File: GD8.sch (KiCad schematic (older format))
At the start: 19 parts, among them IC10 IXDD614PI, IC9 HCPL-316J, P8 CONN_01X03, P9 CONN_01X03

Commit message: uding HCPL-361J modified symbol
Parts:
- IC9: symbol HCPL-316J-RESCUE-gatedrive -> HCPL-316J
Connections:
- wire segments 41 -> 50
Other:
- moved on the sheet: IC10
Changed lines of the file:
@@
 EESchema Schematic File Version 2
-LIBS:gatedrive-rescue
 LIBS:power
 LIBS:device
@@
 LIBS:contrib
 LIBS:valves
-LIBS:GateDrive
+LIBS:74xgxx
+LIBS:ac-dc
+LIBS:actel
+LIBS:Altera
+LIBS:analog_devices
+LIBS:brooktre
+LIBS:cmos_ieee
+LIBS:dc-dc
+LIBS:diode
+LIBS:elec-unifil
+LIBS:ESD_Protection
+LIBS:ftdi
+LIBS:gennum
+LIBS:graphic
+LIBS:hc11
+LIBS:ir
+LIBS:Lattice
+LIBS:logo
+LIBS:maxim
+LIBS:microchip_dspic33dsc
+LIBS:microchip_pic10mcu
+LIBS:microchip_pic12mcu
+LIBS:microchip_pic16mcu
+LIBS:microchip_pic18mcu
+LIBS:microchip_pic32mcu
+LIBS:motor_drivers
+LIBS:msp430
+LIBS:nordicsemi
+LIBS:nxp_armmcu
+LIBS:onsemi
+LIBS:Oscillators
+LIBS:powerint
+LIBS:Power_Management
+LIBS:pspice
+LIBS:references
+LIBS:relays
+LIBS:rfcom
+LIBS:sensors
+LIBS:silabs
+LIBS:stm8
+LIBS:stm32
+LIBS:supertex
+LIBS:switches
+LIBS:transf
+LIBS:ttl_ieee
+LIBS:video
+LIBS:Worldsemi
+LIBS:Xicor
+LIBS:Zilog
 LIBS:gatedrive-cache
 EELAYER 25 0
@@
 L IXDD614PI-RESCUE-gatedrive IC10
 U 1 1 56EFD9AC
-P 7900 5100
-F 0 "IC10" H 7900 4900 60  0000 C CNN
-F 1 "IXDD614PI" H 7950 5450 60  0000 C CNN
-F 2 "gatedrive:DIP-8_W7.62mm_LongPads" H 7900 5200 60  0001 C CNN
-F 3 "" H 7900 5200 60  0000 C CNN
-F 4 "CHINA[already bought]" H 7900 5100 60  0001 C CNN "Supplier"
-	1    7900 5100
-	1    0    0    -1
-$EndComp
-$Comp
-L HCPL-316J-RESCUE-gatedrive IC9
+P 7950 5100
+AR Path="/56EFD9AC" Ref="IC10"  Part="1"
+AR Path="/56EF0569/56EFD9AC" Ref="IC10"  Part="1"
+F 0 "IC10" H 7950 4900 60  0000 C CNN
+F 1 "IXDD614PI" H 8000 5450 60  0000 C CNN
+F 2 "gatedrive:DIP-8_W7.62mm_LongPads" H 7950 5200 60  0001 C CNN
+F 3 "" H 7950 5200 60  0000 C CNN
+F 4 "CHINA[already bought]" H 7950 5100 60  0001 C CNN "Supplier"
+	1    7950 5100
+	1    0    0    -1
+$EndComp
+$Comp
+L HCPL-316J IC9
 U 1 1 56EFD9AD
-P 5550 4750
-F 0 "IC9" H 5550 4150 60  0000 C CNN
-F 1 "HCPL-316J" H 5300 5200 60  0000 C CNN
-F 2 "Housings_SOIC:SOIC-16_7.5x10.3mm_Pitch1.27mm" H 5550 4750 60  0001 C CNN
-F 3 "" H 5550 4750 60  0000 C CNN
-F 4 "CHINA [ already bought]" H 5550 4750 60  0001 C CNN "Supplier"
-	1    5550 4750
+P 5600 4850
+F 0 "IC9" H 5350 4450 60  0000 C CNN
+F 1 "HCPL-316J" H 5400 5350 60  0000 C CNN
+F 2 "Housings_SOIC:SOIC-16_7.5x10.3mm_Pitch1.27mm" H 5600 4850 60  0001 C CNN
+F 3 "" H 5600 4850 60  0000 C CNN
+F 4 "CHINA [ already bought]" H 5600 4850 60  0001 C CNN "Supplier"
+	1    5600 4850
 	1    0    0    -1
 $EndComp
@@
 Text GLabel 6450 4800 2    60   Input ~ 0
 15V8
-Text GLabel 7500 4850 0    60   Input ~ 0
-15V8
-Text GLabel 7500 5150 0    60   Input ~ 0
--5v8
-Text GLabel 8350 5150 2    60   Input ~ 0
+Text GLabel 7550 4850 0    60   Input ~ 0
+15V8
+Text GLabel 7550 5150 0    60   Input ~ 0
+-5v8
+Text GLabel 8300 5150 2    60   Input ~ 0
 -5v8
 Text GLabel 10200 4950 2    60   Input ~ 0
@@
 a cap to ensure soft turn-off, recommended by datasheet of hcpl.
 Wire Wire Line
-	6950 4950 7500 4950
-Wire Wire Line
-	6250 4950 6650 4950
-Wire Wire Line
-	6250 5050 6250 5150
-Wire Wire Line
-	6250 4750 6250 4850
+	6950 4950 7150 4950
+Wire Wire Line
+	7150 4950 7550 4950
+Wire Wire Line
+	5800 4950 6500 4950
+Wire Wire Line
+	6500 4950 6650 4950
+Wire Wire Line
+	5800 5050 6250 5100
+Wire Wire Line
+	6250 5100 5800 5150
+Wire Wire Line
+	5800 4750 6250 4800
+Wire Wire Line
+	6250 4800 5800 4850
 Connection ~ 6550 4100
 Wire Wire Line
-	6550 4650 6250 4650
+	6550 4650 5800 4650
 Wire Wire Line
 	6550 4100 6650 4100
 Wire Wire Line
-	6550 4050 6550 4650
+	6550 4050 6550 4100
+Wire Wire Line
+	6550 4100 6550 4650
 Connection ~ 8450 4950
 Wire Wire Line
@@
 Connection ~ 7150 4950
 Wire Wire Line
-	3625 4650 4850 4650
-Wire Wire Line
-	8350 4950 9050 4950
+	3625 4650 4000 4650
+Wire Wire Line
+	4000 4650 4900 4650
+Wire Wire Line
+	8300 4950 8450 4950
+Wire Wire Line
+	8450 4950 8900 4950
+Wire Wire Line
+	8900 4950 9050 4950
 Wire Wire Line
 	9350 4950 9450 4950
 Wire Wire Line
-	9750 4950 10200 4950
+	9750 4950 9950 4950
+Wire Wire Line
+	9950 4950 10200 4950
 Wire Wire Line
 	9750 5250 9950 5250
@@
 Connection ~ 9950 4950
 Wire Wire Line
-	8350 5050 8450 5050
+	8300 5050 8450 5050
 Wire Wire Line
 	8450 5050 8450 4950
@@
 	4400 4350 4400 4550
 Wire Wire Line
-	4400 4550 4850 4550
+	4400 4550 4900 4550
 Wire Wire Line
 	4000 4350 4000 4650
@@
 	4000 5300 4000 4750
 Wire Wire Line
-	4000 4750 4850 4750
-Wire Wire Line
-	4850 5150 4750 5150
+	4000 4750 4900 4750
+Wire Wire Line
+	4900 5150 4750 5150
 Wire Wire Line
 	4750 5150 4750 5300
 Wire Wire Line
-	4850 4850 4400 4850
+	4900 4850 4400 4850
 Wire Wire Line
 	4400 4850 4400 5300
 Wire Wire Line
-	6250 4450 6300 4450
+	5800 4450 6300 4450
 Wire Wire Line
 	6300 4450 6300 4350
@@
 Wire Wire Line
 	6500 5000 6500 4950
-Text GLabel 8350 4850 2    60   Input ~ 0
+Text GLabel 8300 4850 2    60   Input ~ 0
 15V8
 Text GLabel 7175 5075 3    60   Input ~ 0
 15V8
 Wire Wire Line
-	7500 5050 7175 5050
+	7550 5050 7175 5050
 Wire Wire Line
 	7175 5050 7175 5075
 Text HLabel 900  3800 3    60   Input ~ 0
 T8
-Text HLabel 4850 4450 0    60   Input ~ 0
+Text HLabel 4900 4450 0    60   Input ~ 0
 T8
 Text GLabel 4750 5300 3    60   Input ~ 0
 GND1
-Text GLabel 4850 4950 0    60   Input ~ 0
+Text GLabel 4900 4950 0    60   Input ~ 0
 ~FAULT
 Text GLabel 4400 5300 3    60   Input ~ 0

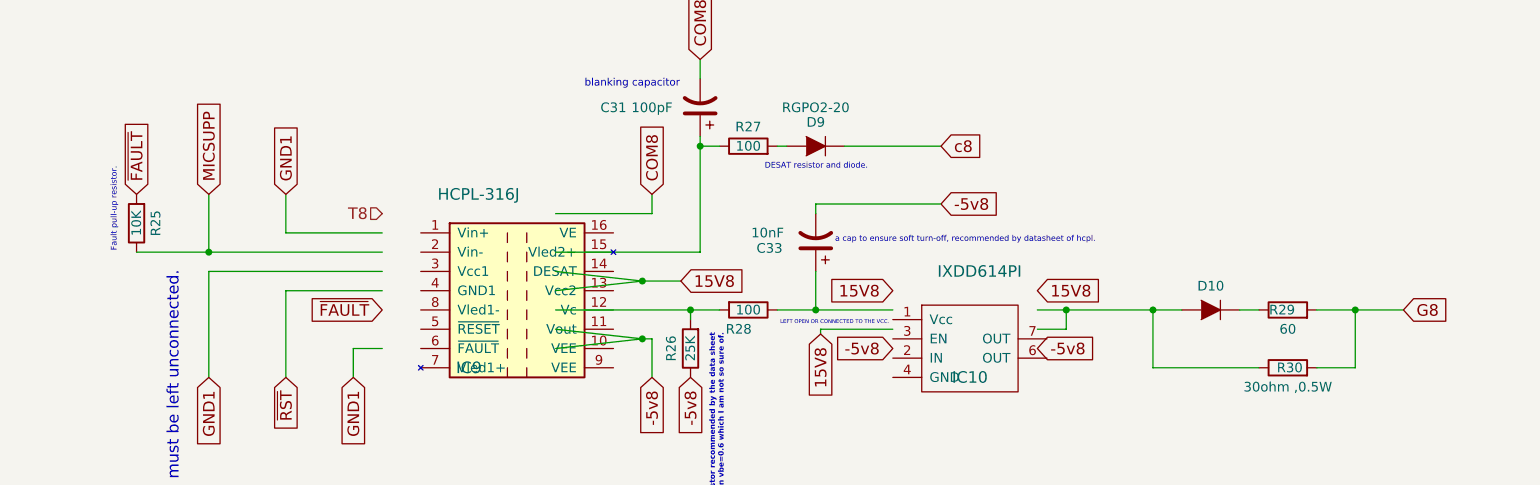
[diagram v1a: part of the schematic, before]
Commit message: cleaning the schematic
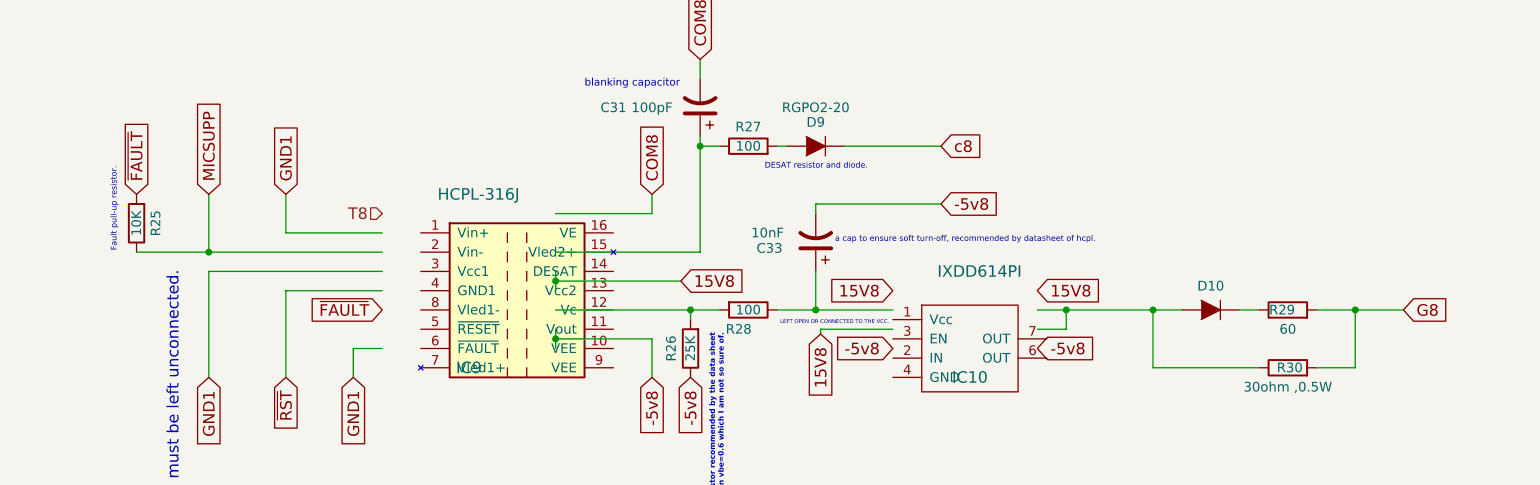
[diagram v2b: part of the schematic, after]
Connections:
- wire segments 50 -> 41
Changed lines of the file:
@@
 a cap to ensure soft turn-off, recommended by datasheet of hcpl.
 Wire Wire Line
-	6950 4950 7150 4950
+	6950 4950 7550 4950
 Wire Wire Line
-	7150 4950 7550 4950
+	5800 4950 6650 4950
 Wire Wire Line
-	5800 4950 6500 4950
+	5800 5050 5800 5150
 Wire Wire Line
-	6500 4950 6650 4950
-Wire Wire Line
-	5800 5050 6250 5100
-Wire Wire Line
-	6250 5100 5800 5150
-Wire Wire Line
-	5800 4750 6250 4800
-Wire Wire Line
-	6250 4800 5800 4850
+	5800 4750 5800 4850
 Connection ~ 6550 4100
 Wire Wire Line
@@
 	6550 4100 6650 4100
 Wire Wire Line
-	6550 4050 6550 4100
-Wire Wire Line
-	6550 4100 6550 4650
+	6550 4050 6550 4650
 Connection ~ 8450 4950
 Wire Wire Line
@@
 Connection ~ 7150 4950
 Wire Wire Line
-	3625 4650 4000 4650
+	3625 4650 4900 4650
 Wire Wire Line
-	4000 4650 4900 4650
-Wire Wire Line
-	8300 4950 8450 4950
-Wire Wire Line
-	8450 4950 8900 4950
-Wire Wire Line
-	8900 4950 9050 4950
+	8300 4950 9050 4950
 Wire Wire Line
 	9350 4950 9450 4950
 Wire Wire Line
-	9750 4950 9950 4950
-Wire Wire Line
-	9950 4950 10200 4950
+	9750 4950 10200 4950
 Wire Wire Line
 	9750 5250 9950 5250
@@
 	6300 5300 6300 5100
 Wire Wire Line
-	6300 5100 6250 5100
-Connection ~ 6250 5100
+	6300 5100 5800 5100
+Connection ~ 5800 5100
 Wire Wire Line
-	6250 4800 6450 4800
-Connection ~ 6250 4800
+	5800 4800 6450 4800
+Connection ~ 5800 4800
 Wire Wire Line
 	8900 5250 9450 5250

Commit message: completion of the layout, initial layout of the protection circuit, reducing number of circuit to 7
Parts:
- C29, C30, C31, C32, C33, C34, C35: footprint Capacitors_ThroughHole:C_Disc_D3_P2.5 -> gatedrive:C_Disc
- D9: footprint Diodes_ThroughHole:Diode_DO-201AD_Horizontal_RM15 -> Diodes_ThroughHole:Diode_DO-41_SOD81_Horizontal_RM10
- R25: footprint Resistors_ThroughHole:Resistor_Vertical_RM5mm -> Resistors_ThroughHole:Resistor_Horizontal_RM10mm
- R29, R30: footprint Resistors_ThroughHole:Resistor_Horizontal_RM20mm -> gatedrive:Resistor_multi
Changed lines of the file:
@@
 EESchema Schematic File Version 2
+LIBS:Symbols_DCDC-ACDC-Converter_RevC_20Jul2012
+LIBS:Symbols_EN60617_13Mar2013
+LIBS:Symbols_EN60617-10_HF-Radio_DRAFT_12Sep2013
+LIBS:Symbols_ICs-Diskrete_RevD10
+LIBS:Symbols_ICs-Opto_RevB_16Sep2013
+LIBS:Symbols_Microcontroller_Philips-NXP_RevA_06Oct2013
+LIBS:SymbolsSimilarEN60617+oldDIN617-RevE8
+LIBS:Symbols_Socket-DIN41612_RevA
+LIBS:Symbols_Transformer-Diskrete_RevA
 LIBS:power
 LIBS:device
@@
 $Descr A4 11693 8268
 encoding utf-8
-Sheet 6 10
+Sheet 6 9
 Title "IGBT GATE DRIVE SCHEMATIC."
 Date "2016-03-02"
@@
 F 0 "D9" H 7150 3976 50  0000 C CNN
 F 1 "RGPO2-20" H 7150 3900 50  0000 C CNN
-F 2 "Diodes_ThroughHole:Diode_DO-201AD_Horizontal_RM15" H 7150 4100 50  0001 C CNN
+F 2 "Diodes_ThroughHole:Diode_DO-41_SOD81_Horizontal_RM10" H 7150 4100 50  0001 C CNN
 F 3 "" H 7150 4100 50  0000 C CNN
 F 4 "El-Amir" H 7150 4100 60  0001 C CNN "Supplier"
@@
 F 0 "R25" V 3525 4500 50  0000 C CNN
 F 1 "10K" V 3625 4500 50  0000 C CNN
-F 2 "Resistors_ThroughHole:Resistor_Vertical_RM5mm" V 3555 4500 50  0001 C CNN
+F 2 "Resistors_ThroughHole:Resistor_Horizontal_RM10mm" V 3555 4500 50  0001 C CNN
 F 3 "" H 3625 4500 50  0000 C CNN
 F 4 "EL AMIR" H 3625 4500 60  0001 C CNN "Supplier"
@@
 F 0 "C29" H 4150 2150 50  0000 C CNN
 F 1 "0.1uF" H 4250 2050 50  0000 C CNN
-F 2 "Capacitors_ThroughHole:C_Disc_D3_P2.5" H 4488 2000 50  0001 C CNN
+F 2 "gatedrive:C_Disc" H 4488 2000 50  0001 C CNN
 F 3 "" H 4450 2150 50  0000 C CNN
 F 4 "EL AMIR" H 4450 2150 60  0001 C CNN "Supplier"
@@
 F 0 "C31" H 7000 3900 50  0000 C CNN
 F 1 "100pF" H 6800 3900 50  0000 C CNN
-F 2 "Capacitors_ThroughHole:C_Disc_D3_P2.5" H 6588 3750 50  0001 C CNN
+F 2 "gatedrive:C_Disc" H 6588 3750 50  0001 C CNN
 F 3 "" H 6550 3900 50  0000 C CNN
 	1    6550 3900
@@
 F 0 "C35" H 8450 2150 50  0000 C CNN
 F 1 "0.1uF" H 8450 2050 50  0000 C CNN
-F 2 "Capacitors_ThroughHole:C_Disc_D3_P2.5" H 8888 2000 50  0001 C CNN
+F 2 "gatedrive:C_Disc" H 8888 2000 50  0001 C CNN
 F 3 "" H 8850 2150 50  0000 C CNN
 	1    8850 2150
@@
 F 0 "C34" H 7400 2150 50  0000 C CNN
 F 1 "0.1uF" H 7400 2050 50  0000 C CNN
-F 2 "Capacitors_ThroughHole:C_Disc_D3_P2.5" H 7788 2000 50  0001 C CNN
+F 2 "gatedrive:C_Disc" H 7788 2000 50  0001 C CNN
 F 3 "" H 7750 2150 50  0000 C CNN
 	1    7750 2150
@@
 F 0 "C30" H 5150 2150 50  0000 C CNN
 F 1 "0.1uF" H 5150 2050 50  0000 C CNN
-F 2 "Capacitors_ThroughHole:C_Disc_D3_P2.5" H 5538 2000 50  0001 C CNN
+F 2 "gatedrive:C_Disc" H 5538 2000 50  0001 C CNN
 F 3 "" H 5500 2150 50  0000 C CNN
 	1    5500 2150
@@
 F 0 "C32" H 6300 2150 50  0000 R CNN
 F 1 "330pF" H 6400 2050 50  0000 R CNN
-F 2 "Capacitors_ThroughHole:C_Disc_D3_P2.5" H 6638 2000 50  0001 C CNN
+F 2 "gatedrive:C_Disc" H 6638 2000 50  0001 C CNN
 F 3 "" H 6600 2150 50  0000 C CNN
 	1    6600 2150
@@
 LEFT OPEN OR CONNECTED TO THE VCC.
 $Comp
-L PWR_FLAG #FLG029
+L PWR_FLAG #FLG043
 U 1 1 56EFD9BA
 P 1300 3800
-F 0 "#FLG029" H 1300 3895 50  0001 C CNN
+F 0 "#FLG043" H 1300 3895 50  0001 C CNN
 F 1 "PWR_FLAG" H 1300 4024 50  0000 C CNN
 F 2 "" H 1300 3800 50  0000 C CNN
@@
 $EndComp
 $Comp
-L PWR_FLAG #FLG030
+L PWR_FLAG #FLG044
 U 1 1 56EFD9BB
 P 1750 3800
-F 0 "#FLG030" H 1750 3895 50  0001 C CNN
+F 0 "#FLG044" H 1750 3895 50  0001 C CNN
 F 1 "PWR_FLAG" H 1750 4024 50  0000 C CNN
 F 2 "" H 1750 3800 50  0000 C CNN
@@
 $EndComp
 $Comp
-L PWR_FLAG #FLG031
+L PWR_FLAG #FLG045
 U 1 1 56EFD9BC
 P 1750 2650
-F 0 "#FLG031" H 1750 2745 50  0001 C CNN
+F 0 "#FLG045" H 1750 2745 50  0001 C CNN
 F 1 "PWR_FLAG" H 1750 2874 50  0000 C CNN
 F 2 "" H 1750 2650 50  0000 C CNN
@@
 $EndComp
 $Comp
-L PWR_FLAG #FLG032
+L PWR_FLAG #FLG046
 U 1 1 56EFD9BD
 P 900 2650
-F 0 "#FLG032" H 900 2745 50  0001 C CNN
+F 0 "#FLG046" H 900 2745 50  0001 C CNN
 F 1 "PWR_FLAG" H 900 2874 50  0000 C CNN
 F 2 "" H 900 2650 50  0000 C CNN
@@
 $EndComp
 $Comp
-L PWR_FLAG #FLG033
+L PWR_FLAG #FLG047
 U 1 1 56EFD9BE
 P 1300 2650
-F 0 "#FLG033" H 1300 2745 50  0001 C CNN
+F 0 "#FLG047" H 1300 2745 50  0001 C CNN
 F 1 "PWR_FLAG" H 1300 2874 50  0000 C CNN
 F 2 "" H 1300 2650 50  0000 C CNN
@@
 $EndComp
 $Comp
-L PWR_FLAG #FLG034
+L PWR_FLAG #FLG048
 U 1 1 56EFD9BF
 P 900 3800
-F 0 "#FLG034" H 900 3895 50  0001 C CNN
+F 0 "#FLG048" H 900 3895 50  0001 C CNN
 F 1 "PWR_FLAG" H 900 4024 50  0000 C CNN
 F 2 "" H 900 3800 50  0000 C CNN
@@
 F 0 "C33" H 7390 4630 50  0000 C CNN
 F 1 "10nF" H 7400 4550 50  0000 C CNN
-F 2 "Capacitors_ThroughHole:C_Disc_D3_P2.5" H 7188 4450 50  0001 C CNN
+F 2 "gatedrive:C_Disc" H 7188 4450 50  0001 C CNN
 F 3 "" H 7150 4600 50  0000 C CNN
 	1    7150 4600
@@
 F 0 "R29" V 9600 4980 50  0000 C CNN
 F 1 "60" V 9500 4950 50  0000 C CNN
-F 2 "Resistors_ThroughHole:Resistor_Horizontal_RM20mm" V 9530 4950 50  0001 C CNN
+F 2 "gatedrive:Resistor_multi" V 9530 4950 50  0001 C CNN
 F 3 "" H 9600 4950 50  0000 C CNN
 F 4 "Al amir" H 9600 4950 60  0001 C CNN "Supplier"
@@
 F 0 "R30" V 9600 5240 50  0000 C CNN
 F 1 "30ohm ,0.5W" V 9500 5250 50  0000 C CNN
-F 2 "Resistors_ThroughHole:Resistor_Horizontal_RM20mm" V 9530 5250 50  0001 C CNN
+F 2 "gatedrive:Resistor_multi" V 9530 5250 50  0001 C CNN
 F 3 "" H 9600 5250 50  0000 C CNN
 F 4 "Supplier_name" H 9600 5250 60  0001 C CNN "Supplier"
@@
 	6950 4100 7000 4100
 $Comp
-L PWR_FLAG #FLG035
+L PWR_FLAG #FLG049
 U 1 1 56EFD9C6
 P 1475 3050
-F 0 "#FLG035" H 1475 3145 50  0001 C CNN
+F 0 "#FLG049" H 1475 3145 50  0001 C CNN
 F 1 "PWR_FLAG" V 1625 3050 50  0000 C CNN
 F 2 "" H 1475 3050 50  0000 C CNN

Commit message: yet another enhancements .
the protection section still is incomplete.
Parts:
- IC10: symbol IXDD614PI-RESCUE-gatedrive -> IXDD614PI
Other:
- moved on the sheet: IC9
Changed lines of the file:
@@
 $Descr A4 11693 8268
 encoding utf-8
-Sheet 6 9
+Sheet 9 9
 Title "IGBT GATE DRIVE SCHEMATIC."
 Date "2016-03-02"
@@
 $EndDescr
 $Comp
-L IXDD614PI-RESCUE-gatedrive IC10
+L IXDD614PI IC10
 U 1 1 56EFD9AC
-P 7950 5100
+P 7950 4950
 AR Path="/56EFD9AC" Ref="IC10"  Part="1"
 AR Path="/56EF0569/56EFD9AC" Ref="IC10"  Part="1"
-F 0 "IC10" H 7950 4900 60  0000 C CNN
-F 1 "IXDD614PI" H 8000 5450 60  0000 C CNN
-F 2 "gatedrive:DIP-8_W7.62mm_LongPads" H 7950 5200 60  0001 C CNN
-F 3 "" H 7950 5200 60  0000 C CNN
-F 4 "CHINA[already bought]" H 7950 5100 60  0001 C CNN "Supplier"
-	1    7950 5100
+F 0 "IC10" H 7950 4750 60  0000 C CNN
+F 1 "IXDD614PI" H 7950 5300 60  0000 C CNN
+F 2 "gatedrive:DIP-8_W7.62mm_LongPads" H 7950 5050 60  0001 C CNN
+F 3 "" H 7950 5050 60  0000 C CNN
+F 4 "CHINA[already bought]" H 7950 4950 60  0001 C CNN "Supplier"
+	1    7950 4950
 	1    0    0    -1
 $EndComp
@@
 L HCPL-316J IC9
 U 1 1 56EFD9AD
-P 5600 4850
-F 0 "IC9" H 5350 4450 60  0000 C CNN
-F 1 "HCPL-316J" H 5400 5350 60  0000 C CNN
-F 2 "Housings_SOIC:SOIC-16_7.5x10.3mm_Pitch1.27mm" H 5600 4850 60  0001 C CNN
-F 3 "" H 5600 4850 60  0000 C CNN
-F 4 "CHINA [ already bought]" H 5600 4850 60  0001 C CNN "Supplier"
-	1    5600 4850
+P 5300 4750
+AR Path="/56EFD9AD" Ref="IC9"  Part="1"
+AR Path="/56EF0569/56EFD9AD" Ref="IC9"  Part="1"
+F 0 "IC9" H 5300 4250 60  0000 C CNN
+F 1 "HCPL-316J" H 5350 5200 60  0000 C CNN
+F 2 "Housings_SOIC:SOIC-16_7.5x10.3mm_Pitch1.27mm" H 5300 4750 60  0001 C CNN
+F 3 "" H 5300 4750 60  0000 C CNN
+F 4 "CHINA [ already bought]" H 5300 4750 60  0001 C CNN "Supplier"
+	1    5300 4750
 	1    0    0    -1
 $EndComp
@@
 Text GLabel 7550 5150 0    60   Input ~ 0
 -5v8
-Text GLabel 8300 5150 2    60   Input ~ 0
+Text GLabel 8350 5150 2    60   Input ~ 0
 -5v8
 Text GLabel 10200 4950 2    60   Input ~ 0
@@
 Connection ~ 7150 4950
 Wire Wire Line
-	3625 4650 4900 4650
-Wire Wire Line
-	8300 4950 9050 4950
+	3625 4650 4800 4650
+Wire Wire Line
+	8350 4950 9050 4950
 Wire Wire Line
 	9350 4950 9450 4950
@@
 Connection ~ 9950 4950
 Wire Wire Line
-	8300 5050 8450 5050
+	8350 5050 8450 5050
 Wire Wire Line
 	8450 5050 8450 4950
@@
 	4400 4350 4400 4550
 Wire Wire Line
-	4400 4550 4900 4550
+	4400 4550 4800 4550
 Wire Wire Line
 	4000 4350 4000 4650
@@
 	4000 5300 4000 4750
 Wire Wire Line
-	4000 4750 4900 4750
-Wire Wire Line
-	4900 5150 4750 5150
+	4000 4750 4800 4750
+Wire Wire Line
+	4800 5150 4750 5150
 Wire Wire Line
 	4750 5150 4750 5300
 Wire Wire Line
-	4900 4850 4400 4850
+	4800 4850 4400 4850
 Wire Wire Line
 	4400 4850 4400 5300
@@
 Wire Wire Line
 	6500 5000 6500 4950
-Text GLabel 8300 4850 2    60   Input ~ 0
+Text GLabel 8350 4850 2    60   Input ~ 0
 15V8
 Text GLabel 7175 5075 3    60   Input ~ 0
@@
 Text HLabel 900  3800 3    60   Input ~ 0
 T8
-Text HLabel 4900 4450 0    60   Input ~ 0
+Text HLabel 4800 4450 0    60   Input ~ 0
 T8
 Text GLabel 4750 5300 3    60   Input ~ 0
 GND1
-Text GLabel 4900 4950 0    60   Input ~ 0
+Text GLabel 4800 4950 0    60   Input ~ 0
 ~FAULT
 Text GLabel 4400 5300 3    60   Input ~ 0

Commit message: packup
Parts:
- C29, C30, C31, C32, C33, C34, C35: symbol CP1 -> C_Small
- R25, R26, R27, R28, R29, R30: symbol R -> R_Small
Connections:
- net -5v8: now also C35.1; no longer C34.2, IC10.5 (GND)
- net 15V8: now also C34.2, IC10.3 (EN); no longer C35.1, IC10.2 (IN), IC10.8 (VCC)
- net ~FAULT: now also IC9.6 (~FAULT), R25.1; no longer IC9.5 (~RESET), R25.2
- net ~RST: now also IC9.5 (~RESET); no longer IC9.8 (Vled1-)
- net at C33.1, R28.1: now also IC10.2 (IN); no longer IC10.3 (EN)
- net GND1 renamed GND
- net GND: now also IC9.8 (Vled1-); no longer IC9.7 (Vled1+)
- net MICSUPP renamed +5V
- net +5V: now also R25.2; no longer R25.1
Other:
- note added: "5 volt is the vcc of the microcontroller.\n"
- note added: "GND is the ground of the microcontroller.\n"
- note added: "IN PIN IS LEFT OPEN OR CONNECTED TO THE VCC."
- note added: "a cap to ensure soft turn-off,\n recommended by datasheet of hcpl."
- note removed: "Fault pull-up resistor."
- note removed: "GND1 is the ground of the microcontroller.\n"
- note removed: "I'M USING GLOBAL LABELS INSTEAD OF LOCAL LABELS AS THEY LOOK NEATER, LOL."
- note removed: "LEFT OPEN OR CONNECTED TO THE VCC."
- note removed: "MICSUPP is 5 volt from the vcc of the microcontroller.\n"
- note removed: "a cap to ensure soft turn-off, recommended by datasheet of hcpl."
- moved on the sheet: D10, D9, IC10, IC9, R25, R26, R27, R28, R29, R30
